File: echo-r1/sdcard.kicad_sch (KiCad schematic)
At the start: 6 parts, among them J3 TF-115

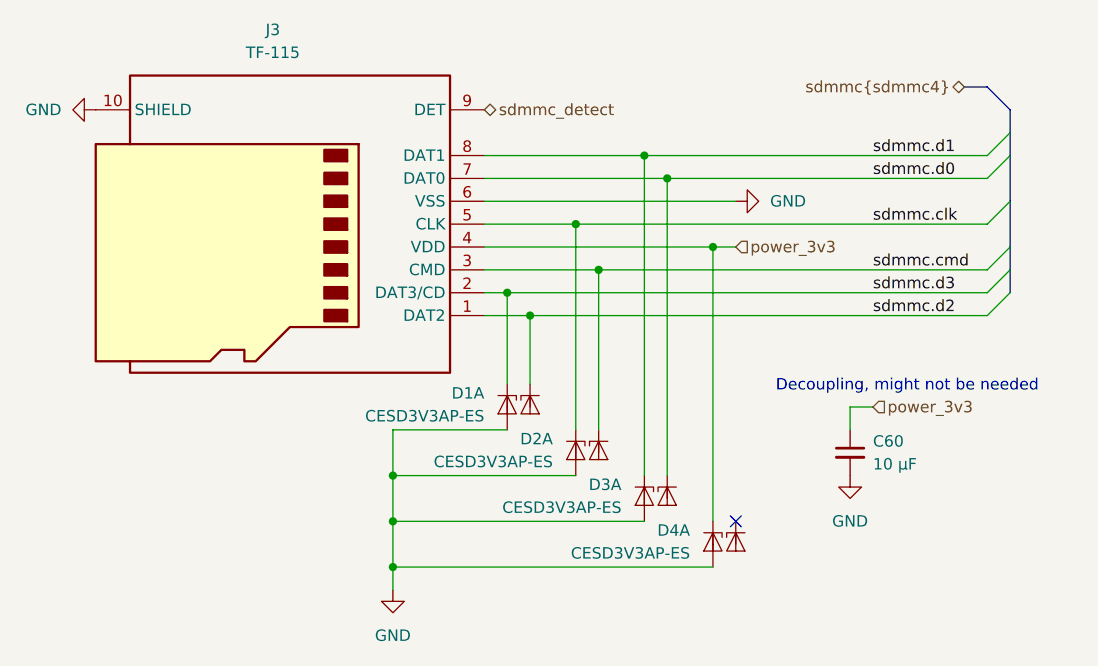
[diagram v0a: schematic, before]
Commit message: WIP redesign with STM32H7R3Z8J6
The H7R3 has a bunch of features that greatly simplify the design:
support for HyperRAM, which requires far fewer pins than SDRAM and
is more power efficient; this frees up the FMC to interface with the
display in 8-bit 8080 MCU mode; and there is a built-in USB HS PHY,
removing the need for an external PHY.

The huge reduction in signal count allows for a smaller pin count
package -- only 144 pins. HyperRAM only comes in BGA packages so it
makes sense to also use the UFBGA-144 package for the CPU, which
takes up less than 1/4 of the board area of an LQFP-176 package.
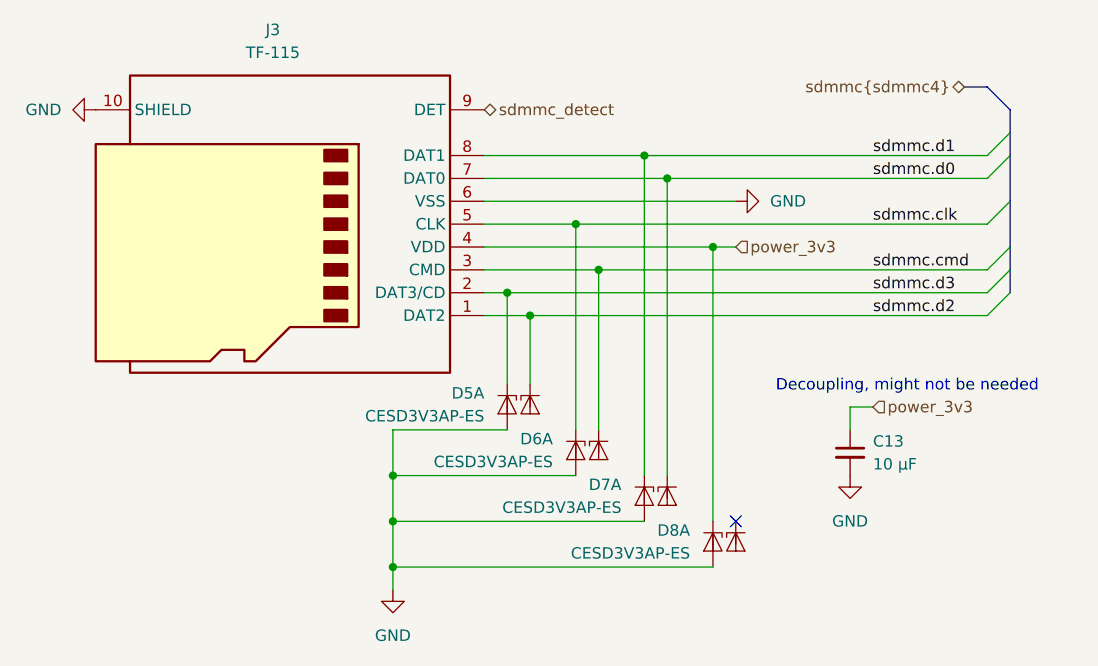
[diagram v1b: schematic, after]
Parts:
- renumbered C60 to C13, D1 to D5, D2 to D6, D3 to D7, D4 to D8
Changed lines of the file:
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@@
 		(dnp no)
 		(fields_autoplaced yes)
-		(property "Reference" "D4"
+		(property "Reference" "D8"
 			(at 172.72 130.5559 90)
 			(effects
@@
 			(project "echo-r1"
 				(path "/aa241847-30f4-429d-a148-6a6e39ba98e0/36f6adaf-1713-488c-a8b8-43e5711e2802"
-					(reference "D4")
+					(reference "D8")
 					(unit 2)
 				)
@@
 		(on_board yes)
 		(dnp no)
-		(property "Reference" "C60"
+		(property "Reference" "C13"
 			(at 185.42 120.6562 0)
 			(effects
@@
 			(project "echo-r1"
 				(path "/aa241847-30f4-429d-a148-6a6e39ba98e0/36f6adaf-1713-488c-a8b8-43e5711e2802"
-					(reference "C60")
+					(reference "C13")
 					(unit 1)
 				)
@@
 		(dnp no)
 		(fields_autoplaced yes)
-		(property "Reference" "#PWR09"
+		(property "Reference" "#PWR027"
 			(at 182.88 130.81 0)
 			(effects
@@
 			(project ""
 				(path "/aa241847-30f4-429d-a148-6a6e39ba98e0/36f6adaf-1713-488c-a8b8-43e5711e2802"
-					(reference "#PWR09")
+					(reference "#PWR027")
 					(unit 1)
 				)
@@
 		(on_board yes)
 		(dnp no)
-		(property "Reference" "D3"
+		(property "Reference" "D7"
 			(at 157.48 125.4759 90)
 			(effects
@@
 			(project "echo-r1"
 				(path "/aa241847-30f4-429d-a148-6a6e39ba98e0/36f6adaf-1713-488c-a8b8-43e5711e2802"
-					(reference "D3")
+					(reference "D7")
 					(unit 1)
 				)
@@
 		(dnp no)
 		(fields_autoplaced yes)
-		(property "Reference" "D3"
+		(property "Reference" "D7"
 			(at 165.1 125.4759 90)
 			(effects
@@
 			(project "echo-r1"
 				(path "/aa241847-30f4-429d-a148-6a6e39ba98e0/36f6adaf-1713-488c-a8b8-43e5711e2802"
-					(reference "D3")
+					(reference "D7")
 					(unit 2)
 				)
@@
 		(dnp no)
 		(fields_autoplaced yes)
-		(property "Reference" "D2"
+		(property "Reference" "D6"
 			(at 157.48 120.3959 90)
 			(effects
@@
 			(project "echo-r1"
 				(path "/aa241847-30f4-429d-a148-6a6e39ba98e0/36f6adaf-1713-488c-a8b8-43e5711e2802"
-					(reference "D2")
+					(reference "D6")
 					(unit 2)
 				)
@@
 		(on_board yes)
 		(dnp no)
-		(property "Reference" "D2"
+		(property "Reference" "D6"
 			(at 149.86 120.3959 90)
 			(effects
@@
 			(project "echo-r1"
 				(path "/aa241847-30f4-429d-a148-6a6e39ba98e0/36f6adaf-1713-488c-a8b8-43e5711e2802"
-					(reference "D2")
+					(reference "D6")
 					(unit 1)
 				)
@@
 		(on_board yes)
 		(dnp no)
-		(property "Reference" "D1"
+		(property "Reference" "D5"
 			(at 142.24 115.3159 90)
 			(effects
@@
 			(project ""
 				(path "/aa241847-30f4-429d-a148-6a6e39ba98e0/36f6adaf-1713-488c-a8b8-43e5711e2802"
-					(reference "D1")
+					(reference "D5")
 					(unit 1)
 				)
@@
 		(dnp no)
 		(fields_autoplaced yes)
-		(property "Reference" "#PWR040"
+		(property "Reference" "#PWR024"
 			(at 92.71 83.82 0)
 			(effects
@@
 			(project ""
 				(path "/aa241847-30f4-429d-a148-6a6e39ba98e0/36f6adaf-1713-488c-a8b8-43e5711e2802"
-					(reference "#PWR040")
+					(reference "#PWR024")
 					(unit 1)
 				)
@@
 		(on_board yes)
 		(dnp no)
-		(property "Reference" "D4"
+		(property "Reference" "D8"
 			(at 165.1 130.5559 90)
 			(effects
@@
 			(project "echo-r1"
 				(path "/aa241847-30f4-429d-a148-6a6e39ba98e0/36f6adaf-1713-488c-a8b8-43e5711e2802"
-					(reference "D4")
+					(reference "D8")
 					(unit 1)
 				)
@@
 		(on_board yes)
 		(dnp no)
-		(property "Reference" "#PWR042"
+		(property "Reference" "#PWR026"
 			(at 176.53 93.98 0)
 			(effects
@@
 			(project ""
 				(path "/aa241847-30f4-429d-a148-6a6e39ba98e0/36f6adaf-1713-488c-a8b8-43e5711e2802"
-					(reference "#PWR042")
+					(reference "#PWR026")
 					(unit 1)
 				)
@@
 		(dnp no)
 		(fields_autoplaced yes)
-		(property "Reference" "D1"
+		(property "Reference" "D5"
 			(at 149.86 115.3159 90)
 			(effects
@@
 			(project ""
 				(path "/aa241847-30f4-429d-a148-6a6e39ba98e0/36f6adaf-1713-488c-a8b8-43e5711e2802"
-					(reference "D1")
+					(reference "D5")
 					(unit 2)
 				)
@@
 		(dnp no)
 		(fields_autoplaced yes)
-		(property "Reference" "#PWR041"
+		(property "Reference" "#PWR025"
 			(at 132.08 143.51 0)
 			(effects
@@
 			(project "echo-r1"
 				(path "/aa241847-30f4-429d-a148-6a6e39ba98e0/36f6adaf-1713-488c-a8b8-43e5711e2802"
-					(reference "#PWR041")
+					(reference "#PWR025")
 					(unit 1)
 				)
